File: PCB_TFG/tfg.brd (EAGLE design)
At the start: 85.1 x 58.4 mm, 11 parts

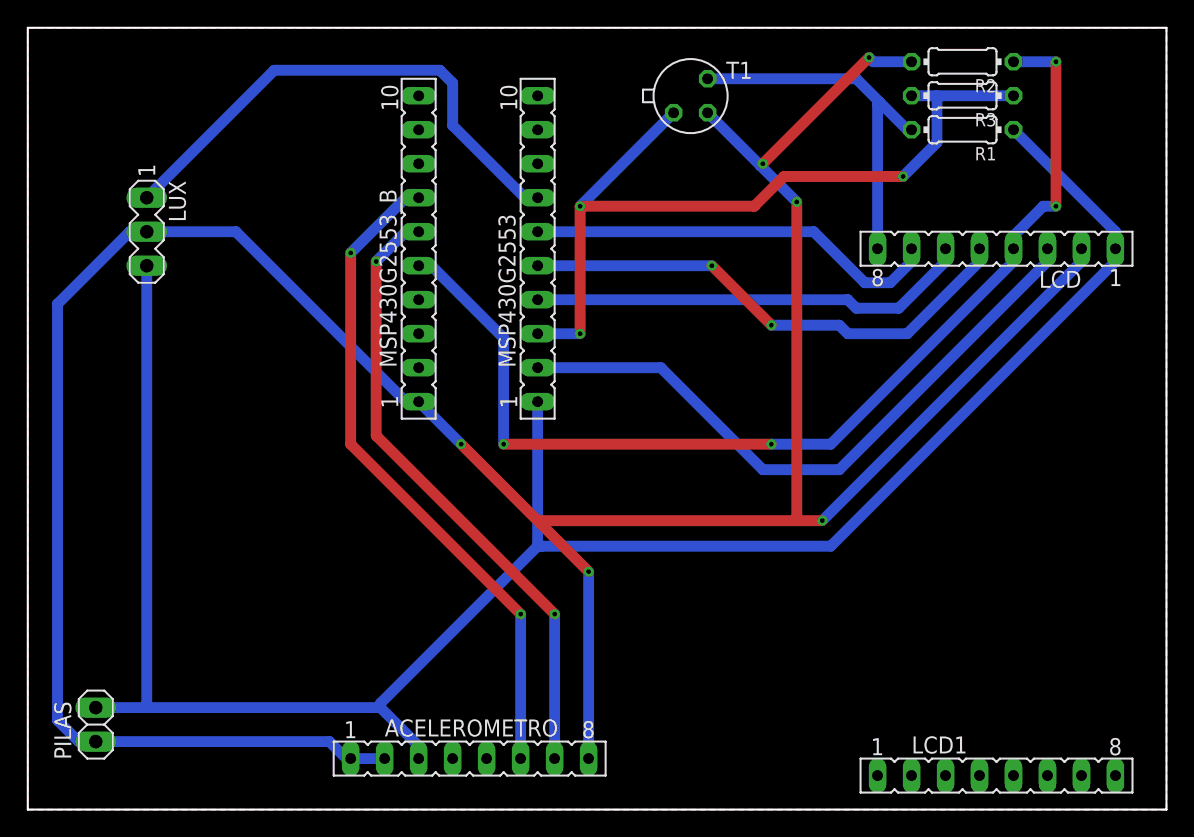
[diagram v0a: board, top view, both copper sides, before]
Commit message: PCB Updated. Waiting check
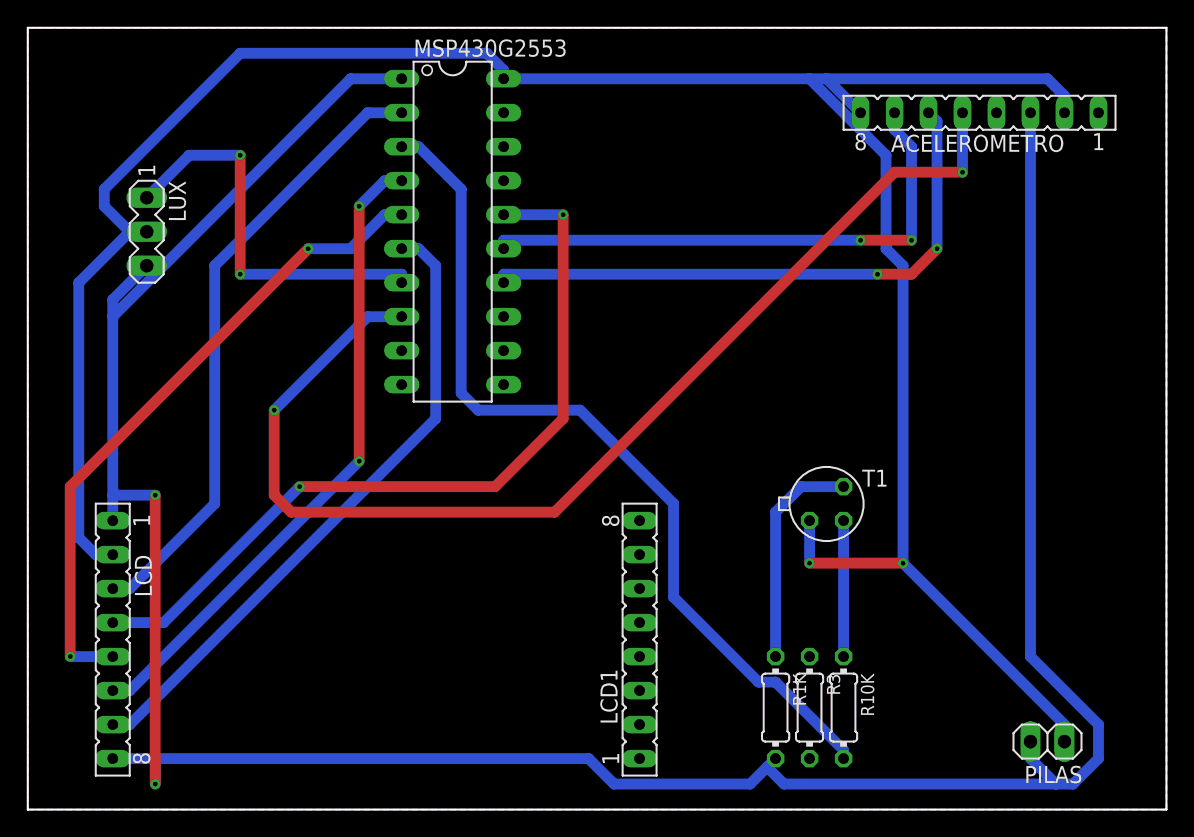
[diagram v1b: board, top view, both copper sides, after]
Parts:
- removed MSP430G2553_B: (no value), con-lsta:FE10
- removed R1, R2: (no value), rcl:0204/7
- added R10K, R1K: (no value), rcl:0204/7
- MSP430G2553: device con-lsta:FE10 -> TI_MSP430_v16:N20
- moved LCD 72.2 mm to (6.35, 12.7), turned to 270 degrees
- moved PILAS 71.1 mm to (76.2, 5.08), turned to 180 degrees
- moved ACELEROMETRO 61.5 mm to (71.1, 52.1), turned to 180 degrees
- moved R3 47.1 mm to (58.4, 7.62), turned to 270 degrees
- moved T1 32.1 mm to (59.7, 22.9)
- moved LCD1 28.5 mm to (45.7, 12.7), turned to 90 degrees
- moved MSP430G2553 6.48 mm to (31.8, 43.2), turned to 270 degrees
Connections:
- net S$3 renamed DO
- removed net LEN: MSP430G2553.3, R3.1, R3.2, T1.1
- removed net V_VCC: ACELEROMETRO.3, LCD.1, LUX.3, MSP430G2553.1, PILAS.2, R1.1
- new net 3V3: ACELEROMETRO.3, LCD.1, LCD.8, LUX.3, MSP430G2553.1, PILAS.2, R1K.2
- new net BASE: R10K.1, T1.2
- new net INT1: ACELEROMETRO.5, MSP430G2553.8
- new net LED_IN: MSP430G2553.3, R10K.2
- net COLECTOR: now also R1K.1; no longer LCD.8, R1.2
- net GND: now also MSP430G2553.20, T1.1; no longer ACELEROMETRO.1, MSP430G2553_B.1, R2.2, T1.2
- net RST: now also MSP430G2553.16; no longer MSP430G2553_B.5, R2.1
- net SCL: now also MSP430G2553.14; no longer MSP430G2553_B.7
- net SDA: now also MSP430G2553.15; no longer MSP430G2553_B.6
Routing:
- net 3V3: track 0.00 -> 207.2 mm, vias 0 -> 2
- net V_VCC: track 152.0 -> 0.00 mm
- net INT1: track 0.00 -> 85.7 mm, vias 0 -> 2
- net LED_IN: track 0.00 -> 65.4 mm
- net LEN: track 62.3 -> 0.00 mm, vias 3 -> 0
- net GND: track 220.7 -> 184.1 mm, vias 6 -> 2
- net RST: track 80.2 -> 59.7 mm, vias 4 -> 2
- net SCLK: track 31.1 -> 48.1 mm
- net DN: track 33.1 -> 48.5 mm, vias 0 -> 2
- net COLECTOR: track 27.8 -> 16.7 mm
- net SDC: track 38.3 -> 49.1 mm
- net BASE: track 0.00 -> 10.2 mm
- net DO: track 39.0 -> 29.9 mm, vias 0 -> 2
- net SCL: track 49.8 -> 44.2 mm
- net SDA: track 46.8 -> 41.2 mm
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- added copper zone on layer 1, net COPPER
- added copper zone on layer 16, net COPPER
- removed copper zone on layer 1, net COOPER
- removed copper zone on layer 16, net COOPER

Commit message: Reset Signal Connected to PULLDOWN
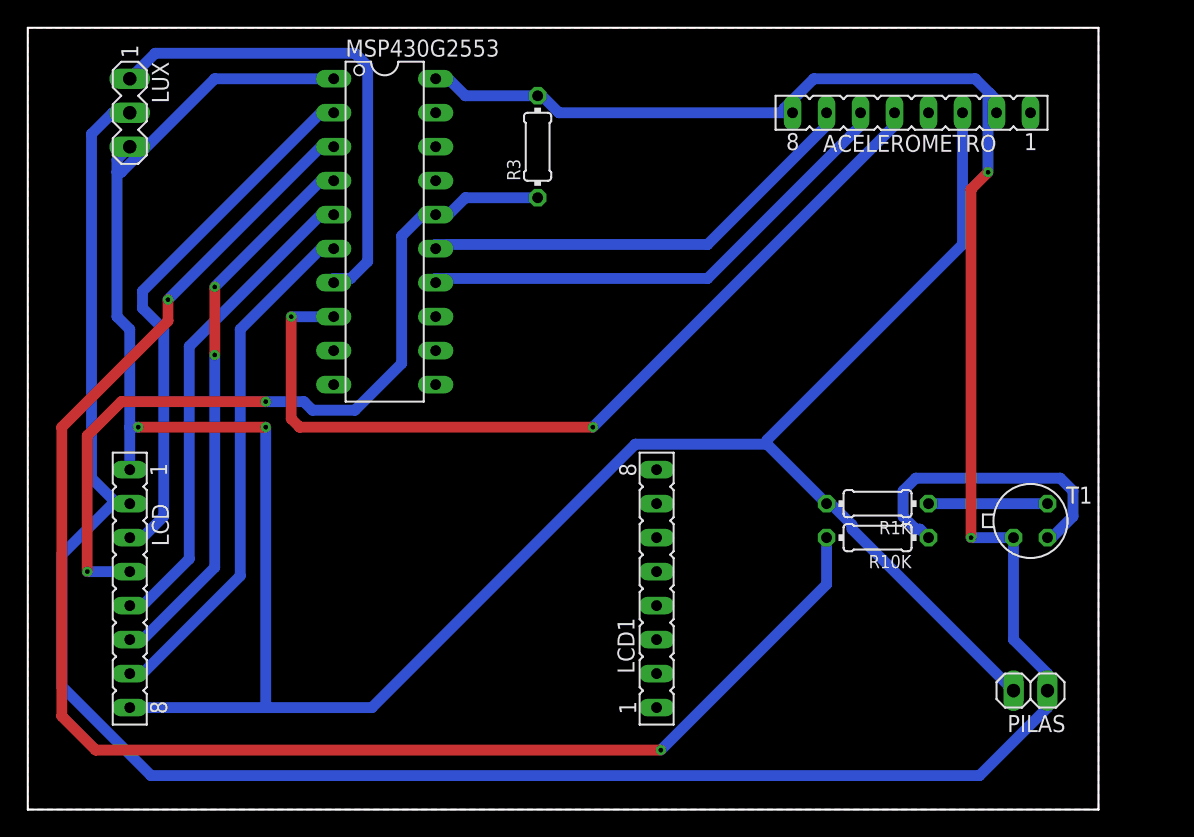
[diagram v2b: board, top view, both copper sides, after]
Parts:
- moved R3 46.6 mm to (38.1, 49.5), turned to 90 degrees
- moved R1K 17.0 mm to (63.5, 22.9), turned to 180 degrees
- moved T1 15.3 mm to (74.9, 21.6)
- moved R10K 13.0 mm to (63.5, 20.3), turned to 180 degrees
- moved LUX 8.98 mm to (7.62, 52.1)
- moved ACELEROMETRO 5.08 mm to (66.0, 52.1)
- moved MSP430G2553 5.08 mm to (26.7, 43.2)
- moved LCD1 4.02 mm to (47.0, 16.5)
- moved LCD 4.02 mm to (7.62, 16.5)
- moved PILAS 4.02 mm to (74.9, 8.89)
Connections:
- net GND: now also R3.2
- net RST: now also R3.1
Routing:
- net LED_IN: track 65.4 -> 118.3 mm, vias 0 -> 2
- net GND: track 184.1 -> 225.4 mm
- net 3V3: track 207.2 -> 187.9 mm
- net INT1: track 85.7 -> 66.4 mm
- net SDC: track 49.1 -> 36.6 mm, vias 2 -> 0
- net BASE: track 10.2 -> 22.4 mm
- net SCLK: track 48.1 -> 39.2 mm
- net COLECTOR: track 16.7 -> 8.89 mm
- net DO: track 29.9 -> 36.9 mm, vias 2 -> 0
- net SDA: track 41.2 -> 34.2 mm, vias 2 -> 0
- net DN: track 48.5 -> 41.7 mm
- net SCL: track 44.2 -> 37.7 mm, vias 2 -> 0
- net SCE: track 46.7 -> 40.5 mm
- net RST: track 59.7 -> 60.5 mm
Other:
- board size 85.1 x 58.4 mm -> 80 x 58.4 mm
